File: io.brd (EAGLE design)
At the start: 23 x 40 mm, 34 parts, among them J1 SJ-3502-SMT-TR, Q1 2SCR574D3TL1, Q2 2SCR574D3TL1, U1 MCP1703T-5002E, U3 LM386M-1, X1 Antenna

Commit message: updating layouts and parts
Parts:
- moved C25 10.5 mm to (15.2, 24.9), turned to 270 degrees
- moved R5 7.73 mm to (12.7, 16.5)
- moved R6 7.73 mm to (10.2, 16.5)
- moved C2 5.99 mm to (12.7, 12.6)
- moved U1 5.36 mm to (3.81, 9.65), turned to 90 degrees
- moved L3 5.24 mm to (8.89, 8.89), turned to 270 degrees
- moved C24 4.58 mm to (10.2, 35.4)
- moved C7 3.81 mm to (15.2, 29.2)
- moved L5 3.81 mm to (15.2, 26.7)
- moved C6 3.81 mm to (15.2, 31.8)
- moved L4 3.45 mm to (18.3, 18.8)
- moved L2 3.39 mm to (19.1, 10.9)
- moved R7 2.67 mm to (19.8, 6.99), flipped to the bottom, turned to 180 degrees
- moved C19 2.54 mm to (11.4, 15.2)
- moved C9 2.54 mm to (11.4, 17.8)
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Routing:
- net GND: track 142.9 -> 0.00 mm
- net OUT_A: track 21.4 -> 34.3 mm
- net 6V_DC: track 15.7 -> 25.6 mm, vias 2 -> 0
- net N$13: track 4.92 -> 13.5 mm, vias 0 -> 2
- net OUT_B: track 25.7 -> 33.5 mm, vias 3 -> 2
- net N$21: track 19.0 -> 11.5 mm, vias 2 -> 1
- net ANT_IN: track 19.7 -> 26.8 mm
- net VIN: track 83.1 -> 76.1 mm, vias 2 -> 1
- net N$14: track 4.36 -> 9.37 mm
- net N$10: track 9.25 -> 13.0 mm
- net N$12: track 4.18 -> 7.84 mm
- net N$24: track 13.6 -> 10.7 mm, vias 2 -> 1
- net N$20: track 8.77 -> 7.24 mm
- net N$25: track 11.9 -> 13.2 mm
- net N$22: track 10.4 -> 9.31 mm, vias 0 -> 1
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
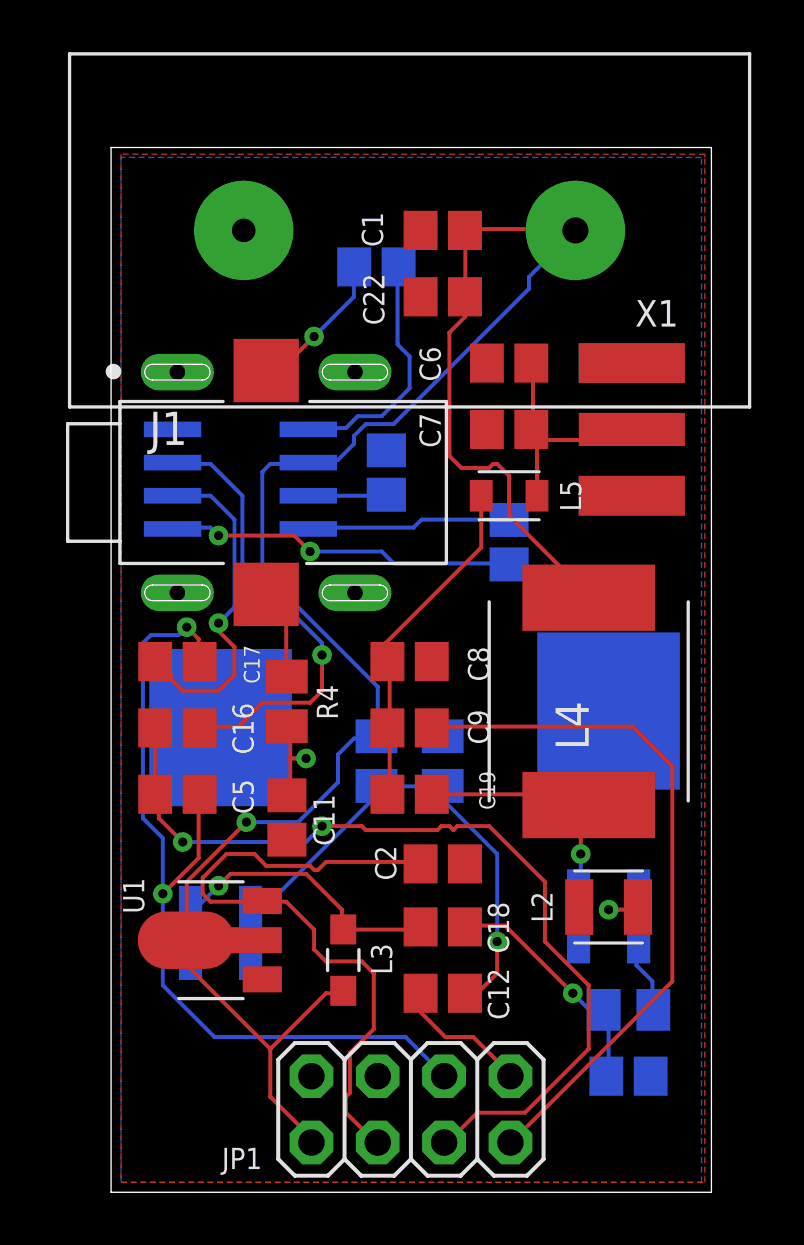
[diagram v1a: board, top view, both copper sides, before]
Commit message: updated Q1, added readme
Updated Q1 to be a better replacement for the original PN2222A in an SMD format. Also added a readme, with links to PNGs of the schematics and layout renderings, as well as a photo of one of my prototypes.
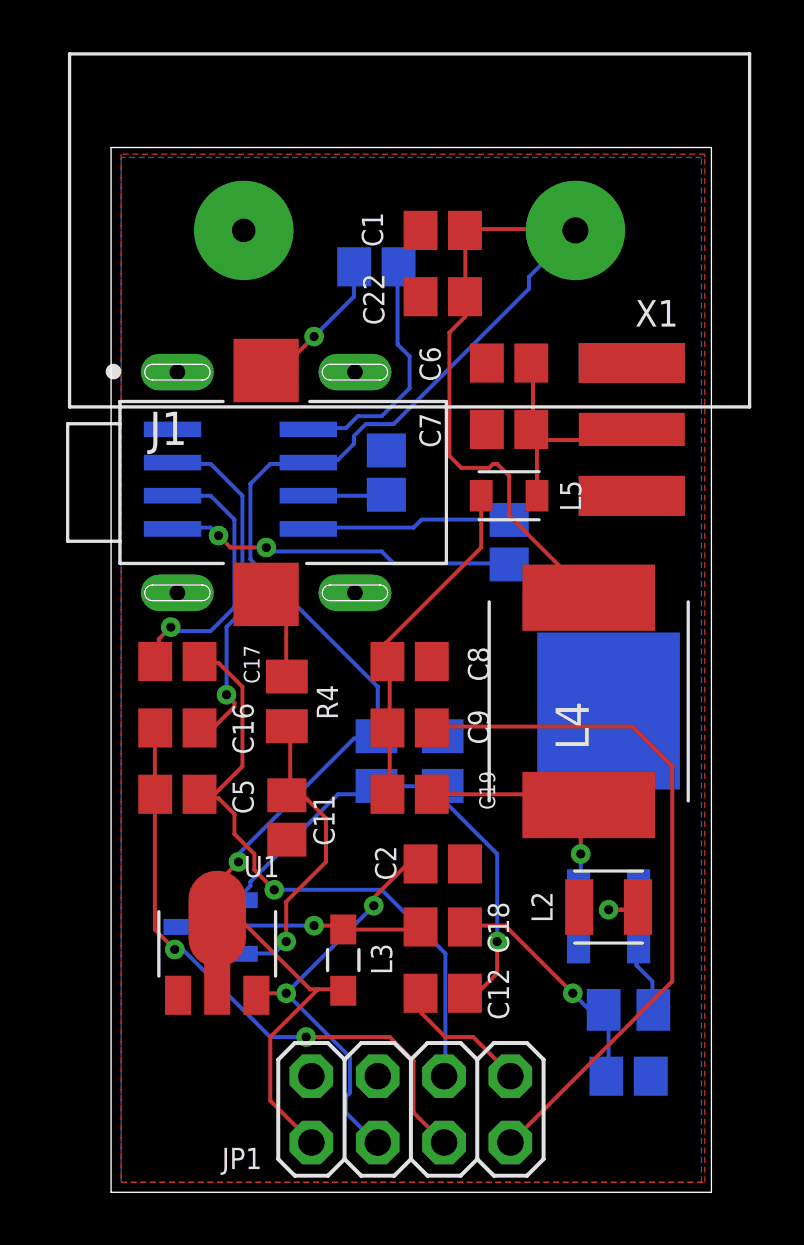
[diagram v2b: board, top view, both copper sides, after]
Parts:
- Q1: value 2SCR574D3TL1 -> MMBT2222A; device zort2:TRANS_2SCR573D_ROM -> zort2:SOT-23_DIO-M
- moved Q1 5.73 mm to (3.81, 10.2), turned to 270 degrees
- moved U1 0.28 mm to (4.06, 9.53), turned to 0 degrees
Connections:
- net N$20: now also Q1.2; no longer Q1.3
- net N$21: now also Q1.3; no longer Q1.2
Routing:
- net OUT_A: track 34.3 -> 23.3 mm
- net 6V_DC: track 25.6 -> 16.0 mm, vias 0 -> 2
- net OUT_B: track 33.5 -> 24.3 mm, vias 2 -> 1
- net N$20: track 7.24 -> 12.2 mm
- net N$9: track 17.2 -> 13.3 mm
- net N$10: track 13.0 -> 10.6 mm
- net VIN: track 76.1 -> 73.7 mm
- net N$21: track 11.5 -> 9.19 mm

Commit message: cleaned up boards, new screenshots
Cleaned up the orientation and text on the boards. Ran them through the OshPark rules, and sent off v1 to get printed
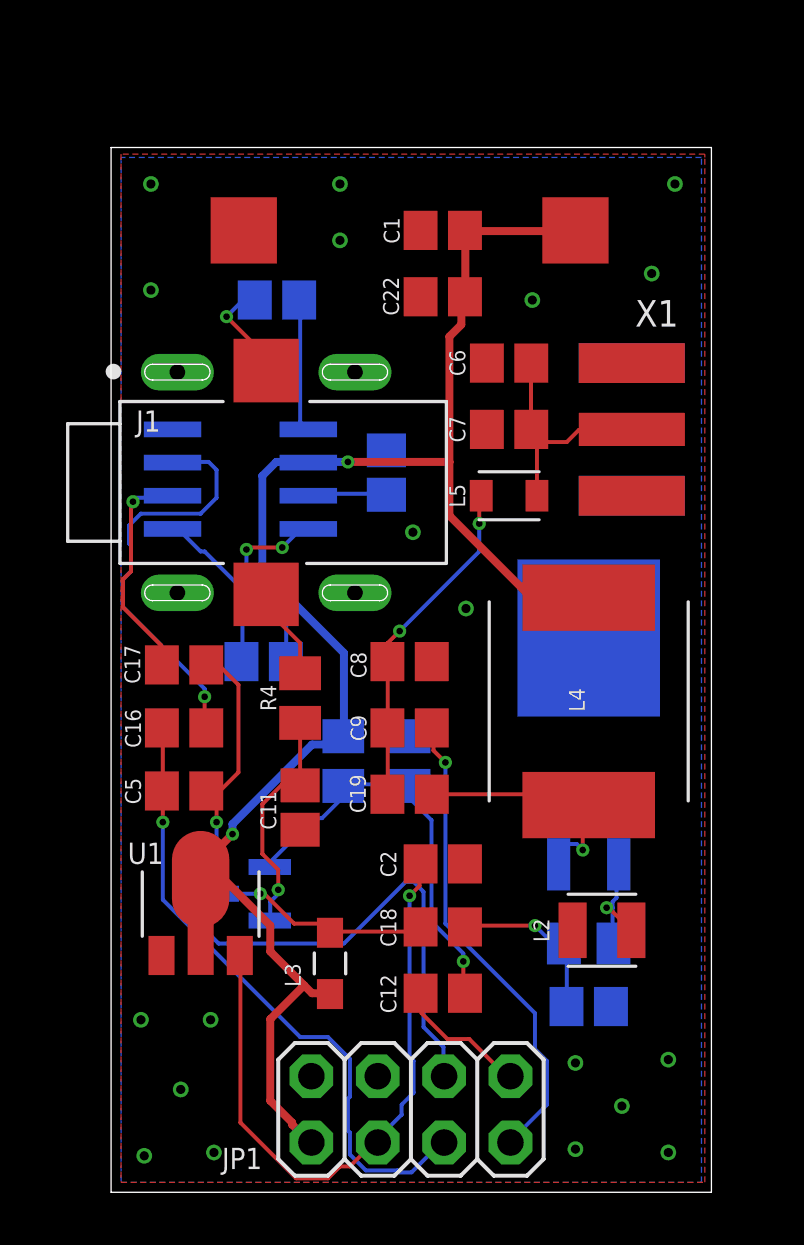
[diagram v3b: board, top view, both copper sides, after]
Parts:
- removed U$2: 9V_968, zort2:9V_968
- added U$1: 9V_9689V_968_SMD, zort2:9V_968_PAD
- C22: value 33u/16V -> 33U
- C23, C24, C25: value 10u/16V -> 10u
- moved C25 10.5 mm to (5.84, 20.3), turned to 0 degrees
- moved C24 4.02 mm to (6.35, 34.2)
- moved C10 3.07 mm to (18.3, 7.11)
- moved R7 2.96 mm to (18.3, 9.53)
- moved Q2 2.90 mm to (18.3, 19.3)
- moved Q1 1.80 mm to (5.08, 11.4)
- moved U1 1.65 mm to (3.43, 11.0)
- moved R5 1.27 mm to (11.4, 16.5)
- moved R6 1.27 mm to (8.89, 16.5)
- moved L2 0.92 mm to (18.8, 10.0)
- moved C11 0.63 mm to (7.24, 14.7)
- moved L3 0.52 mm to (8.38, 8.76)
- moved R4 0.52 mm to (7.24, 18.9)
- moved C5 0.28 mm to (2.79, 15.4)
- moved C17 0.28 mm to (2.79, 20.2)
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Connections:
- net GND: now also U$1.P$2; no longer U$2.P$2
- net VIN: now also U$1.P$1; no longer U$2.P$1
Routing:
- net VIN: track 73.7 -> 64.0 mm, vias 1 -> 2
- net 6V_DC: track 16.0 -> 24.6 mm, vias 2 -> 1
- net ANT_IN: track 26.8 -> 18.4 mm, vias 0 -> 1
- net N$13: track 13.5 -> 6.43 mm, vias 2 -> 0
- net OUT_B: track 24.3 -> 30.2 mm
- net N$14: track 9.37 -> 5.15 mm
- net N$19: track 19.4 -> 16.0 mm
- net N$20: track 12.2 -> 8.99 mm
- net N$22: track 9.31 -> 6.59 mm
- net N$9: track 13.3 -> 15.9 mm
- net N$10: track 10.6 -> 8.65 mm
- net HEADPHONE: track 5.72 -> 4.08 mm
- net N$24: track 10.7 -> 9.05 mm
- net OUT_A: track 23.3 -> 24.4 mm, vias 2 -> 1
- net N$23: track 6.34 -> 5.50 mm
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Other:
- board text added: "9vuTX I/O v1 K6GG"

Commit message: Updated boarts to v1.1
9VuTX Version 1.1

Several adjustments after mockup with V 1.0 of the board. That first version would be non-functional due to a few layout mismatches.

* fixed 2nd transistor layout to actually match part / spec (TO-252)
* rotated potentiometers 180 degrees so they face outward instead toward the middle of the board
* expanded pads of L2 (450uH inductor) to match recommended spec
* replaced phone jack with a true surface mount version (SJ-3523-SMT-TR)
* re-arranged the IO board to allow for the different phone jack
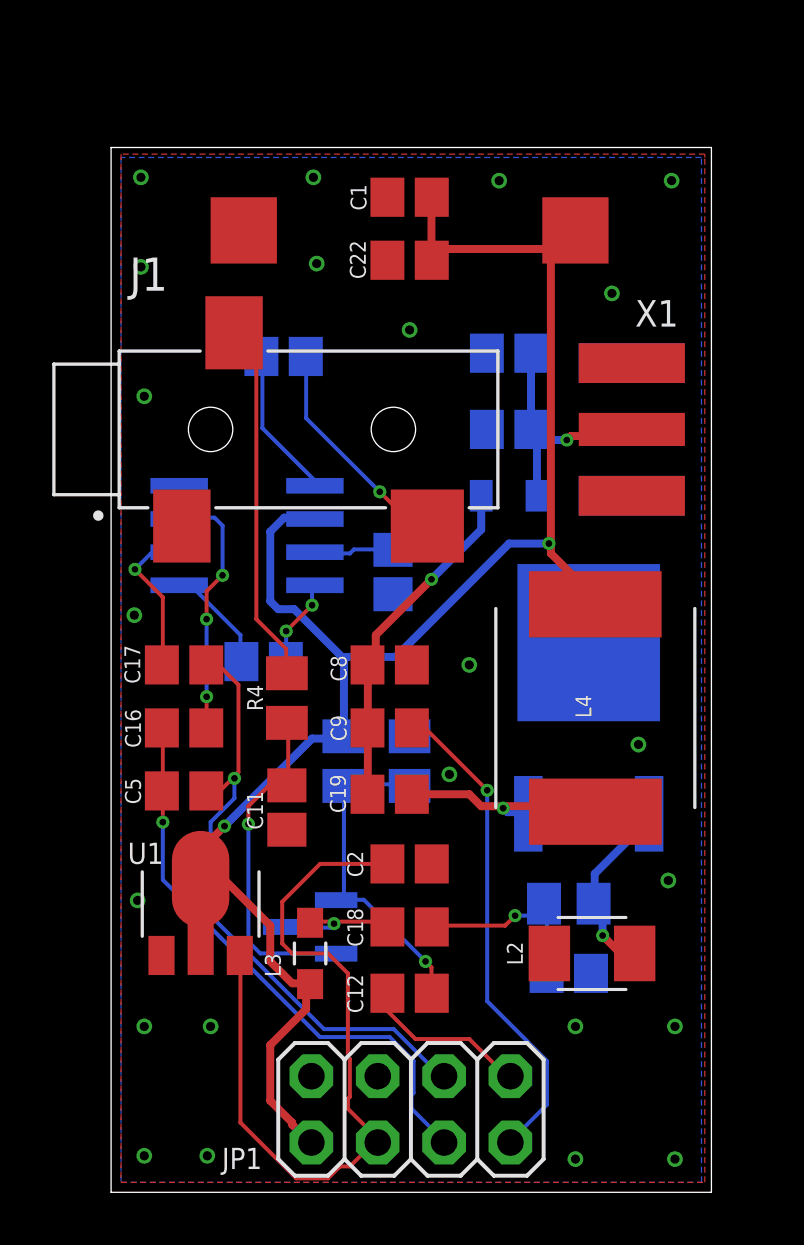
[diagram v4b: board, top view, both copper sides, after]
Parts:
- J1: value SJ-3502-SMT-TR -> SJ-3523-SMT-TR; device Audio Connectors:SJ-3502-SMT-TR -> SJ-3523-SMT-TR:CUI_SJ-3523-SMT-TR
- L2: device Inductor:INDC2520X120N -> zort2:INDC2520X120N
- Q2: value 2SCR574D3TL1 -> 2SCR574D3TL1TRANS_2SCR573_TO-252; device zort2:TRANS_2SCR573D_ROM -> zort2:TO-252
- moved C23 3.82 mm to (10.8, 23.7), turned to 270 degrees
- moved Q1 2.84 mm to (7.62, 10.2)
- moved J1 2.70 mm to (3.81, 29.2)
- moved C24 2.17 mm to (6.60, 32.0), turned to 180 degrees
- moved U3 2.17 mm to (5.21, 25.1)
- moved C22 1.89 mm to (11.4, 35.7)
- moved C1 1.80 mm to (11.4, 38.1)
- moved R7 1.70 mm to (17.5, 11.0)
- moved C10 1.48 mm to (17.5, 8.38)
- moved C12 1.27 mm to (11.4, 7.62)
- moved C18 1.27 mm to (11.4, 10.2)
- moved C2 1.27 mm to (11.4, 12.6)
- moved Q2 1.02 mm to (18.3, 18.3)
- moved L2 0.97 mm to (18.4, 9.14)
- moved L3 0.85 mm to (7.62, 9.14)
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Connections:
- net GND: now also J1.1; no longer J1.1_1, J1.1_2, J1.1_3, J1.1_4
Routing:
- net KEY_IN: track 3.56 -> 13.9 mm
- net OUT_B: track 30.2 -> 23.6 mm
- net N$9: track 15.9 -> 9.81 mm, vias 1 -> 3
- net 6V_DC: track 24.6 -> 29.5 mm, vias 1 -> 0
- net HEADPHONE: track 4.08 -> 8.72 mm
- net N$12: track 7.63 -> 3.40 mm
- net N$20: track 8.99 -> 13.0 mm
- net VIN: track 64.0 -> 67.8 mm
- net N$21: track 8.48 -> 5.16 mm
- net N$19: track 16.0 -> 13.0 mm
- net N$10: track 8.65 -> 6.12 mm
- net OUT_A: track 24.4 -> 22.1 mm
- net N$13: track 6.43 -> 4.17 mm
- net N$23: track 5.50 -> 7.24 mm
- net ANT_OUT: track 5.20 -> 6.43 mm
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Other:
- board text added: "9VuTX IO Board v1.1 K6GG"
- board text removed: "9vuTX I/O v1 K6GG"

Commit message: continuing on v 1.1
* removed "label" label from SMA connector
* increased the width of some lines likely to carry higher current
* attempted to clean up some little stuff
* updated images
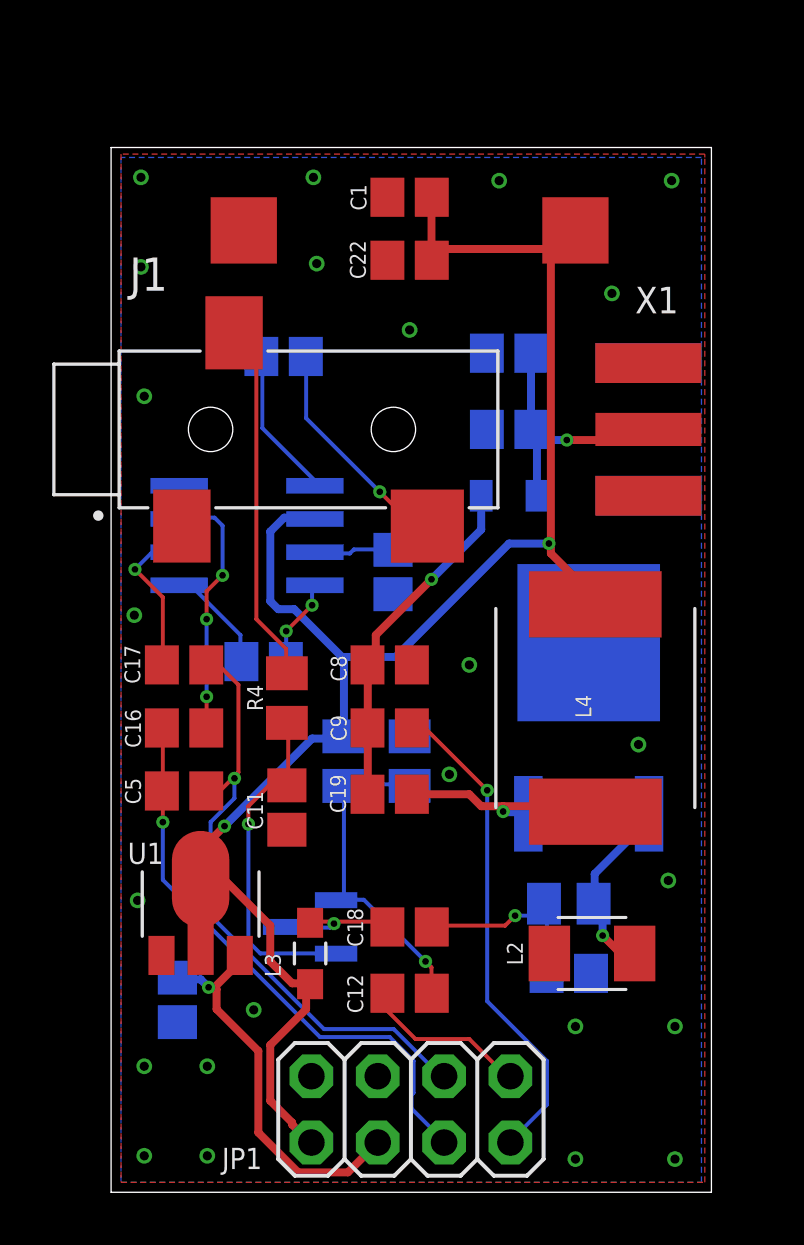
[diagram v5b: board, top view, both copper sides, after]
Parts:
- X1: value Antenna -> (none); device adafruit:SMA_EDGELAUNCH -> zort2:SMA_EDGELAUNCH
- moved C2 10.3 mm to (2.54, 7.37), flipped to the bottom, turned to 270 degrees
- moved X1 0.64 mm to (22.6, 29.2)
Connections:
- new net N$1: X1.GND@2
- new net N$2: X1.GND@4
- net GND: no longer X1.GND@2, X1.GND@4
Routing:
- net 6V_DC: track 29.5 -> 15.1 mm, vias 0 -> 1
- net N$26: track 9.79 -> 11.8 mm
